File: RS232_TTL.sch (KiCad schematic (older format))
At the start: 11 parts, among them J1 TxRx_TTL1, J2 TxRx_TTL2, J3 TxRx232Out2, J4 TxRx232Out1, P1 JmpSim, U1 ST3232E

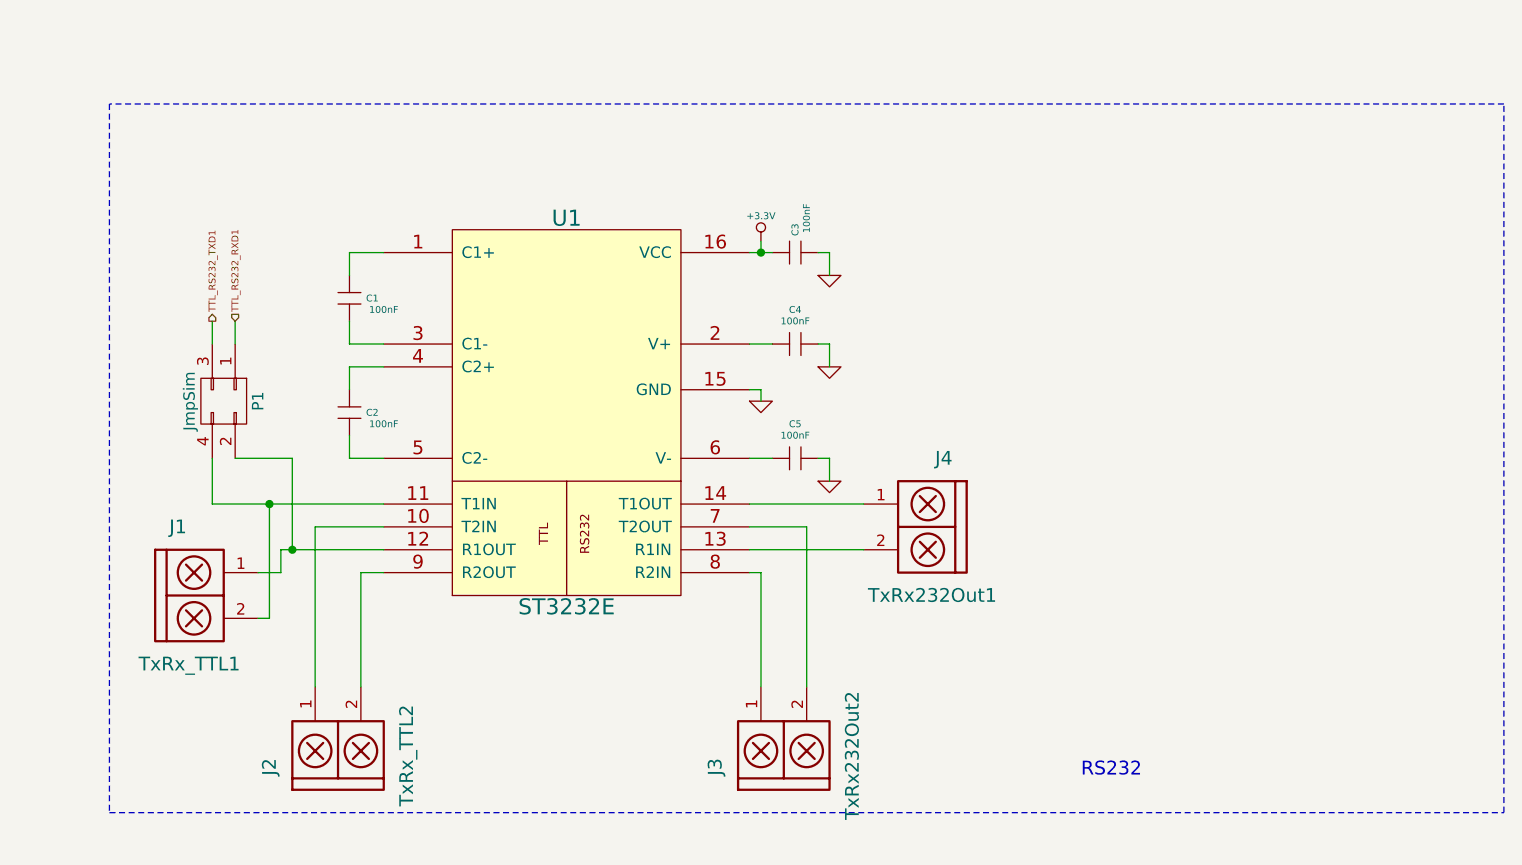
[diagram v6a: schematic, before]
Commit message: Add digikey code and comment schematic.
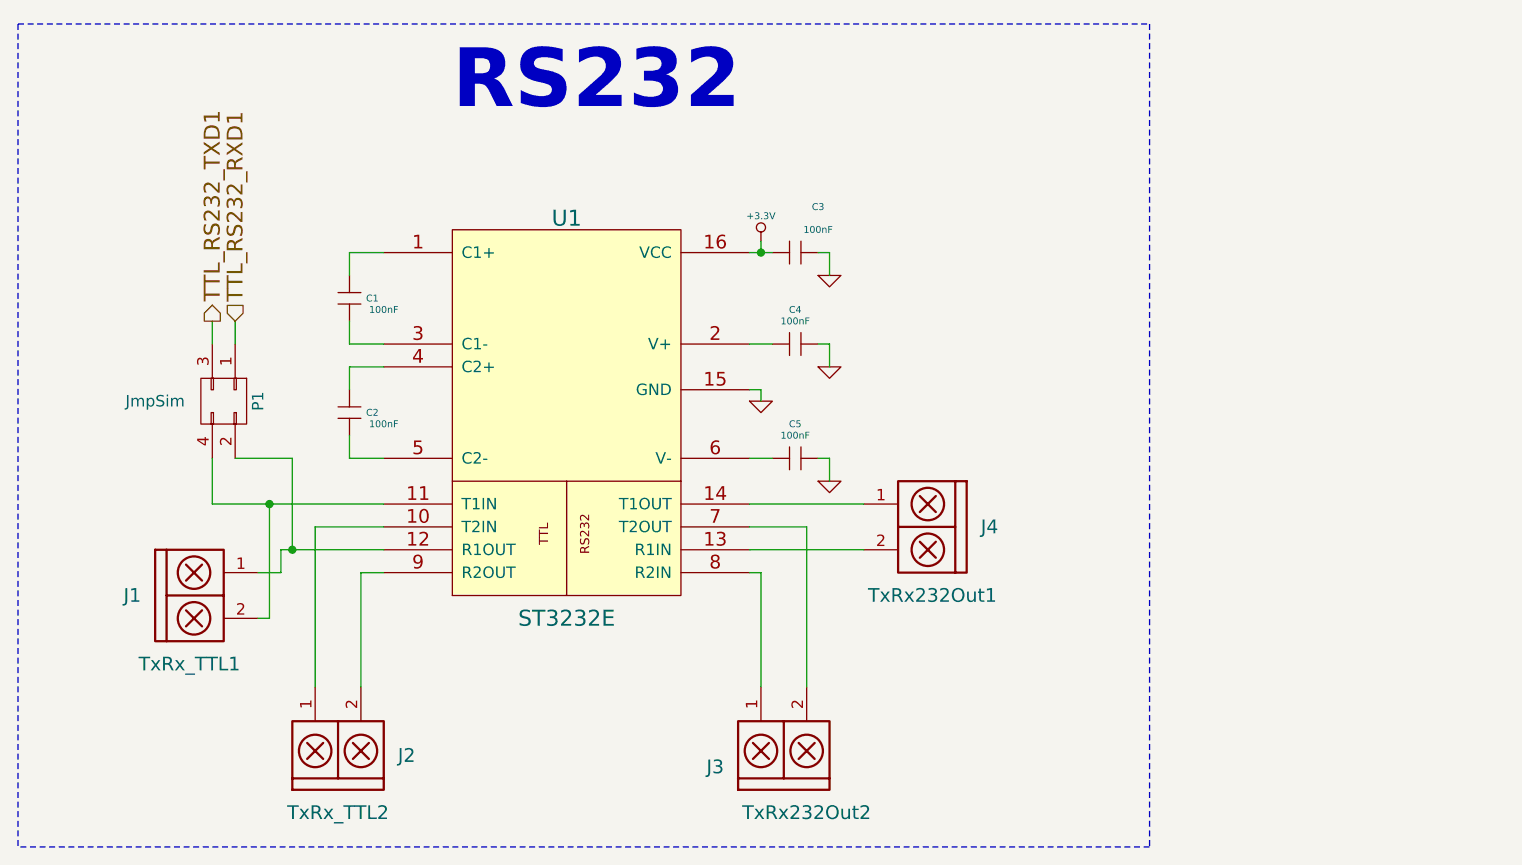
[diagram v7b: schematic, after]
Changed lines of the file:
@@
 LIBS:Oscillators
 LIBS:Power_Management
-LIBS:Worldsemi
 LIBS:Xicor
 LIBS:Zilog
@@
 $EndComp
 $Comp
-L GND-RESCUE-ciaa-nxp #PWR08
+L GND-RESCUE-ciaa-nxp #PWR11
 U 1 1 581A0FB6
 P 5950 3350
-F 0 "#PWR08" H 5950 3350 30  0001 C CNN
+F 0 "#PWR11" H 5950 3350 30  0001 C CNN
 F 1 "GND" H 5950 3280 30  0001 C CNN
 F 2 "" H 5950 3350 60  0000 C CNN
@@
 $EndComp
 $Comp
-L GND-RESCUE-ciaa-nxp #PWR09
+L GND-RESCUE-ciaa-nxp #PWR12
 U 1 1 581A0FB7
 P 5950 3850
-F 0 "#PWR09" H 5950 3850 30  0001 C CNN
+F 0 "#PWR12" H 5950 3850 30  0001 C CNN
 F 1 "GND" H 5950 3780 30  0001 C CNN
 F 2 "" H 5950 3850 60  0000 C CNN
@@
 U 1 1 581A0FB8
 P 5800 2850
-F 0 "C3" V 5800 2950 30  0000 C CNN
-F 1 "100nF" V 5850 3000 30  0000 C CNN
+F 0 "C3" H 5900 3050 30  0000 C CNN
+F 1 "100nF" H 5900 2950 30  0000 C CNN
 F 2 "Capacitors_SMD:C_1206" H 5800 2850 60  0001 C CNN
 F 3 "~" H 5800 2850 60  0000 C CNN
@@
 	1    0    0    -1
 $EndComp
-Text Notes 7050 5150 0    60   ~ 0
+Text Notes 4300 2250 0    257  ~ 51
 RS232
-Text HLabel 3350 3150 1    30   Input ~ 0
+Text HLabel 3350 3150 1    69   Input ~ 0
 TTL_RS232_RXD1
-Text HLabel 3250 3150 1    30   Output ~ 0
+Text HLabel 3250 3150 1    70   Output ~ 0
 TTL_RS232_TXD1
 $Comp
@@
 P 4800 3550
 F 0 "U1" H 4800 4400 70  0000 C CNN
-F 1 "ST3232E" H 4800 2700 70  0000 C CNN
+F 1 "ST3232E" H 4800 2650 70  0000 C CNN
 F 2 "SMD_Packages:SO-16-N" H 4800 3550 60  0001 C CNN
 F 3 "" H 4800 3550 60  0000 C CNN
@@
 $EndComp
 $Comp
-L GND-RESCUE-ciaa-nxp #PWR010
+L GND-RESCUE-ciaa-nxp #PWR9
 U 1 1 581A0FBA
 P 5650 3500
-F 0 "#PWR010" H 5650 3500 30  0001 C CNN
+F 0 "#PWR9" H 5650 3500 30  0001 C CNN
 F 1 "GND" H 5650 3430 30  0001 C CNN
 F 2 "" H 5650 3500 60  0000 C CNN
@@
 $EndComp
 $Comp
-L GND-RESCUE-ciaa-nxp #PWR011
+L GND-RESCUE-ciaa-nxp #PWR10
 U 1 1 581A0FBB
 P 5950 2950
-F 0 "#PWR011" H 5950 2950 30  0001 C CNN
+F 0 "#PWR10" H 5950 2950 30  0001 C CNN
 F 1 "GND" H 5950 2880 30  0001 C CNN
 F 2 "" H 5950 2950 60  0000 C CNN
@@
 $EndComp
 $Comp
-L +3.3V-RESCUE-ciaa-nxp #PWR012
+L +3.3V-RESCUE-ciaa-nxp #PWR8
 U 1 1 581A0FBC
 P 5650 2800
-F 0 "#PWR012" H 5650 2760 30  0001 C CNN
+F 0 "#PWR8" H 5650 2760 30  0001 C CNN
 F 1 "+3.3V" H 5650 2910 30  0000 C CNN
 F 2 "" H 5650 2800 60  0000 C CNN
@@
 U 1 1 581A0FBD
 P 6450 4050
-F 0 "J4" H 6450 4350 60  0000 C CNN
+F 0 "J4" H 6250 4050 60  0000 C CNN
 F 1 "TxRx232Out1" H 6500 3750 60  0000 C CNN
 F 2 "Connect:AK300-2" H 6400 4100 60  0001 C CNN
@@
 P 3300 3500
 F 0 "P1" H 3300 3650 50  0000 C CNN
-F 1 "JmpSim" H 3300 3350 50  0000 C CNN
+F 1 "JmpSim" V 3300 3200 50  0000 C CNN
 F 2 "Pin_Headers:Pin_Header_Straight_2x02" H 3300 2300 50  0001 C CNN
 F 3 "" H 3300 2300 50  0000 C CNN
@@
 U 1 1 581A0FBF
 P 3100 4350
-F 0 "J1" H 3100 4650 60  0000 C CNN
+F 0 "J1" H 2900 4350 60  0000 C CNN
 F 1 "TxRx_TTL1" H 3150 4050 60  0000 C CNN
 F 2 "Connect:AK300-2" H 3050 4400 60  0001 C CNN
@@
 U 1 1 581A0FC0
 P 3800 5100
-F 0 "J2" H 3800 5400 60  0000 C CNN
-F 1 "TxRx_TTL2" H 3850 4800 60  0000 C CNN
+F 0 "J2" V 3850 4800 60  0000 C CNN
+F 1 "TxRx_TTL2" V 3600 5100 60  0000 C CNN
 F 2 "Connect:AK300-2" H 3750 5150 60  0001 C CNN
 F 3 "" H 3750 5150 60  0000 C CNN
@@
 U 1 1 581A0FC1
 P 5750 5100
-F 0 "J3" H 5750 5400 60  0000 C CNN
-F 1 "TxRx232Out2" H 5800 4800 60  0000 C CNN
+F 0 "J3" V 5750 5400 60  0000 C CNN
+F 1 "TxRx232Out2" V 5550 5000 60  0000 C CNN
 F 2 "Connect:AK300-2" H 5700 5150 60  0001 C CNN
 F 3 "" H 5700 5150 60  0000 C CNN
@@
 Wire Wire Line
 	3850 3750 4000 3750
-Wire Notes Line
-	8900 5300 8900 2200
-Wire Notes Line
-	8900 2200 2800 2200
-Wire Notes Line
-	2800 5300 8900 5300
 Wire Wire Line
 	5600 3750 5700 3750
@@
 Wire Wire Line
 	5950 2850 5950 2950
-Wire Notes Line
-	2800 2200 2800 5300
 Wire Wire Line
 	5600 4050 5850 4050
@@
 Wire Wire Line
 	5600 4150 6100 4150
+Wire Notes Line
+	2400 1850 2400 5450
+Wire Notes Line
+	2400 1850 7350 1850
+Wire Notes Line
+	7350 1850 7350 5450
+Wire Notes Line
+	7350 5450 2400 5450
 $EndSCHEMATC
